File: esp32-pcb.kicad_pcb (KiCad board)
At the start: 2 copper layers, 25.2 x 59.4 mm, 47 parts, among them J1 Conn_01x15_Male, J2 Conn_01x15_Male, Q1 TSM2323CX, Q2 BSS138Q-7-F, Q3 MMBT3904, Q4 MMBT3904, SW1 RESET, SW2 USER, SW3 SW_DIP_x04, U1 TLV75533, U2 ESP32-WROOM-32, U3 CP2102N-A01-GQFN24

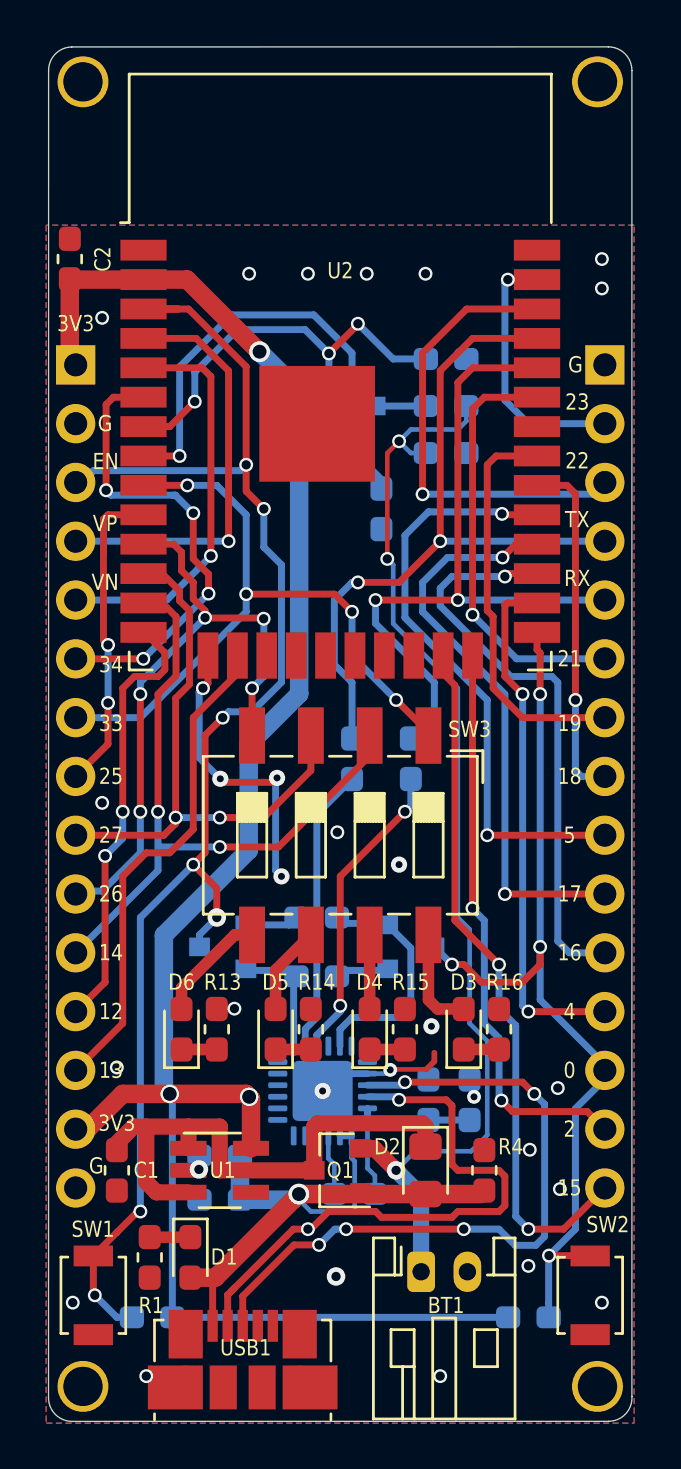
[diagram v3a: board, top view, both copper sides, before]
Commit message: Added TVS protection
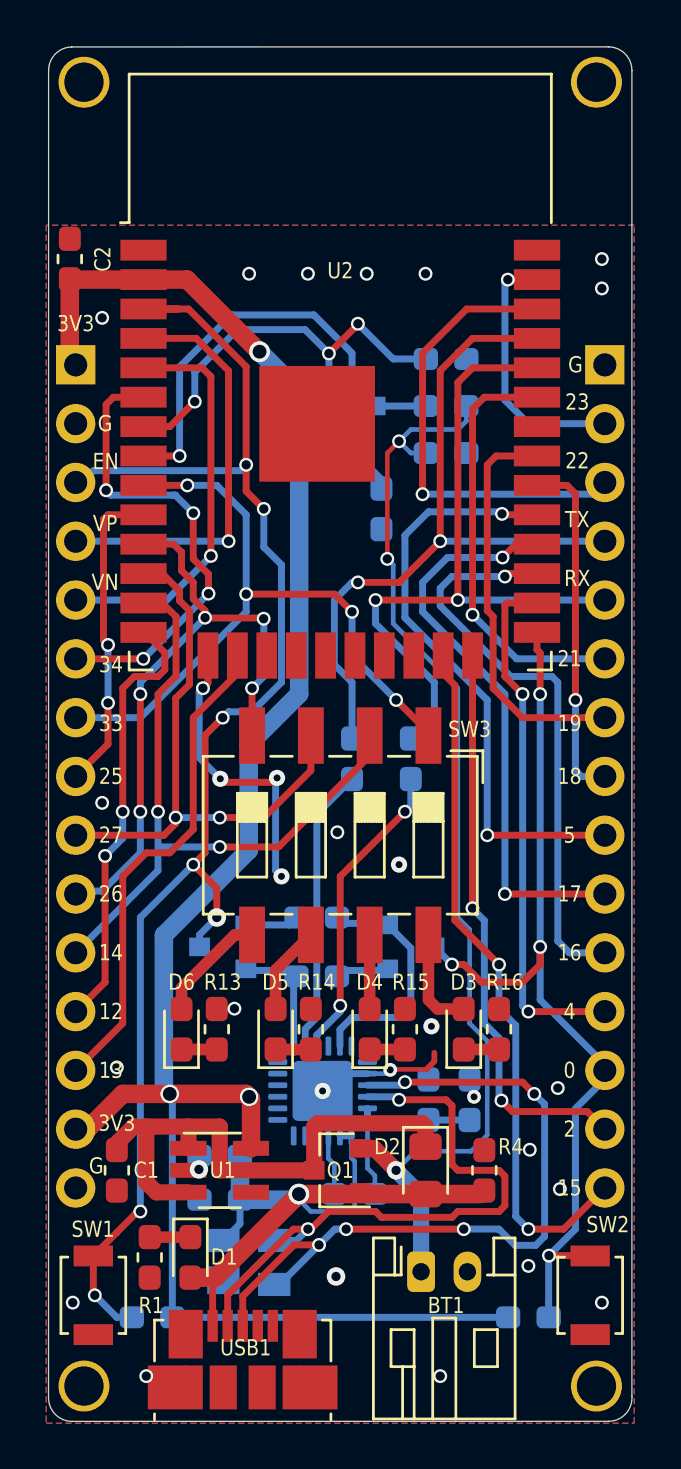
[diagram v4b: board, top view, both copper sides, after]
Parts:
- removed the REF** at (130.6, 126.2)
- removed the REF** at (152.8, 69.8)
- removed the REF** at (152.8, 126.2)
- removed the REF** at (130.6, 69.8)
- added D7: SP0503BAHT, Package_TO_SOT_SMD:SOT-143, B.Cu at (137.8, 120.8)
- added REF**: MountingHole_M1.7, esp32-pcb:MountingHole_M1.7, F.Cu at (152.8, 126.2)
- added REF**: MountingHole_M1.7, esp32-pcb:MountingHole_M1.7, F.Cu at (130.7, 126.2)
- added REF**: MountingHole_M1.7, esp32-pcb:MountingHole_M1.7, F.Cu at (130.7, 69.8)
- added REF**: MountingHole_M1.7, esp32-pcb:MountingHole_M1.7, F.Cu at (152.8, 69.8)
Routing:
- net USB_D+: track 29.9 -> 33.2 mm
- net 5V_USB: track 28.4 -> 30.4 mm
- net USB_D-: track 25.8 -> 27.5 mm
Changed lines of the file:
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@@
     (thickness 1.6)
     (drawings 3056)
-    (tracks 600)
+    (tracks 607)
     (zones 0)
-    (modules 47)
+    (modules 48)
     (nets 74)
   )
@@
   )
   (setup
-    (last_trace_width 0.25)
+    (last_trace_width 0.3)
     (user_trace_width 0.2)
     (user_trace_width 0.25)
@@
     (add_net V_BAT_MEASURE)
   )
-  (module esp32-pcb:MountingHole_M1.7 (layer F.Cu)
-    (at 130.6165 126.1745)
-    (fp_text reference REF** (at 0 -2.54) (layer F.SilkS) hide
+  (module esp32-pcb:MountingHole_M1.7 locked (layer F.Cu)
+    (at 152.8 126.16)
+    (fp_text reference REF** (at 0 -2.54) (layer Dwgs.User) hide
       (effects (font (size 1 1) (thickness 0.15)))
     )
@@
     (pad "" np_thru_hole circle (at 0 0) (size 2.2 2.2) (drill 1.7) (layers *.Cu *.Mask))
   )
-  (module esp32-pcb:MountingHole_M1.7 (layer F.Cu)
-    (at 152.8445 69.8145)
-    (fp_text reference REF** (at 0 -2.54) (layer F.SilkS) hide
+  (module esp32-pcb:MountingHole_M1.7 locked (layer F.Cu)
+    (at 130.66 126.16)
+    (fp_text reference REF** (at 0 -2.54) (layer Dwgs.User) hide
       (effects (font (size 1 1) (thickness 0.15)))
     )
@@
     (pad "" np_thru_hole circle (at 0 0) (size 2.2 2.2) (drill 1.7) (layers *.Cu *.Mask))
   )
-  (module esp32-pcb:MountingHole_M1.7 (layer F.Cu)
-    (at 152.8445 126.1745)
-    (fp_text reference REF** (at 0 -2.54) (layer F.SilkS) hide
+  (module esp32-pcb:MountingHole_M1.7 locked (layer F.Cu)
+    (at 130.66 69.83)
+    (fp_text reference REF** (at 0 -2.54) (layer Dwgs.User) hide
       (effects (font (size 1 1) (thickness 0.15)))
     )
@@
     (pad "" np_thru_hole circle (at 0 0) (size 2.2 2.2) (drill 1.7) (layers *.Cu *.Mask))
   )
-  (module esp32-pcb:MountingHole_M1.7 (layer F.Cu)
-    (at 130.6165 69.8145)
-    (fp_text reference REF** (at 0 -2.54) (layer F.SilkS) hide
+  (module esp32-pcb:MountingHole_M1.7 locked (layer F.Cu)
+    (at 152.8 69.83)
+    (fp_text reference REF** (at 0 -2.54) (layer Dwgs.User) hide
       (effects (font (size 1 1) (thickness 0.15)))
     )
@@
     (pad "" np_thru_hole circle (at 0 0) (size 2.2 2.2) (drill 1.7) (layers *.Cu *.Mask))
   )
+  (module Package_TO_SOT_SMD:SOT-143 (layer B.Cu)
+    (at 137.78 120.82)
+    (descr SOT-143)
+    (tags SOT-143)
+    (attr smd)
+    (fp_text reference D7 (at -0.084 2.1615) (layer B.SilkS)
+      (effects (font (size 0.7 0.6) (thickness 0.15)) (justify mirror))
+    )
+    (fp_text value SP0503BAHT (at -0.28 -2.48) (layer B.Fab)
+      (effects (font (size 1 1) (thickness 0.15)) (justify mirror))
+    )
+    (fp_line (start -2.05 -1.75) (end -2.05 1.75) (layer B.CrtYd) (width 0.05))
+    (fp_line (start -2.05 -1.75) (end 2.05 -1.75) (layer B.CrtYd) (width 0.05))
+    (fp_line (start 2.05 1.75) (end -2.05 1.75) (layer B.CrtYd) (width 0.05))
+    (fp_line (start 2.05 1.75) (end 2.05 -1.75) (layer B.CrtYd) (width 0.05))
+    (fp_line (start 1.2 1.5) (end 1.2 -1.5) (layer B.Fab) (width 0.1))
+    (fp_line (start 1.2 -1.5) (end -1.2 -1.5) (layer B.Fab) (width 0.1))
+    (fp_line (start -1.2 -1.5) (end -1.2 1) (layer B.Fab) (width 0.1))
+    (fp_line (start -0.7 1.5) (end 1.2 1.5) (layer B.Fab) (width 0.1))
+    (fp_line (start -1.2 1) (end -0.7 1.5) (layer B.Fab) (width 0.1))
+    (fp_line (start 1.2 1.55) (end -1.75 1.55) (layer B.SilkS) (width 0.12))
+    (fp_line (start -1.2 -1.55) (end 1.2 -1.55) (layer B.SilkS) (width 0.12))
+    (fp_text user %R (at 0 0 -90) (layer B.Fab)
+      (effects (font (size 0.5 0.5) (thickness 0.075)) (justify mirror))
+    )
+    (pad 4 smd rect (at 1.1 0.95 90) (size 1 1.4) (layers B.Cu B.Paste B.Mask)
+      (net 70 USB_D+))
+    (pad 3 smd rect (at 1.1 -0.95 90) (size 1 1.4) (layers B.Cu B.Paste B.Mask)
+      (net 69 USB_D-))
+    (pad 2 smd rect (at -1.1 -0.95 90) (size 1 1.4) (layers B.Cu B.Paste B.Mask)
+      (net 5 5V_USB))
+    (pad 1 smd rect (at -1.1 0.77 90) (size 1.2 1.4) (layers B.Cu B.Paste B.Mask)
+      (net 1 GND))
+    (model ${KISYS3DMOD}/Package_TO_SOT_SMD.3dshapes/SOT-143.wrl
+      (at (xyz 0 0 0))
+      (scale (xyz 1 1 1))
+      (rotate (xyz 0 0 0))
+    )
+  )
   (module Package_TO_SOT_SMD:SOT-23-5_HandSoldering (layer F.Cu)
     (at 136.525 116.84)
@@
   (segment (start 136.335 121.475) (end 135.255 121.475) (width 0.8) (layer F.Cu) (net 5))
   (segment (start 139.945 117.865) (end 136.335 121.475) (width 0.8) (layer F.Cu) (net 5))
+  (segment (start 137.4 119.15) (end 136.68 119.87) (width 0.3) (layer B.Cu) (net 5))
+  (segment (start 137.4 118.11) (end 137.4 119.15) (width 0.3) (layer B.Cu) (net 5))
   (segment (start 133.5 119.725) (end 135.255 119.725) (width 0.5) (layer F.Cu) (net 6) (status 30))
   (segment (start 147.066 109.869) (end 145.937 109.869) (width 0.5) (layer F.Cu) (net 7) (status 10))
@@
   (segment (start 137.026041 122.062) (end 137.16402 121.92402) (width 0.3) (layer F.Cu) (net 69))
   (segment (start 137.16402 121.92402) (end 139.708041 119.38) (width 0.3) (layer F.Cu) (net 69))
+  (segment (start 139.845 119.87) (end 140.335 119.38) (width 0.3) (layer B.Cu) (net 69))
+  (segment (start 138.88 119.87) (end 139.845 119.87) (width 0.3) (layer B.Cu) (net 69))
   (via (at 140.814952 120.062931) (size 0.6) (drill 0.4) (layers F.Cu B.Cu) (net 70))
   (segment (start 140.922069 120.062931) (end 140.814952 120.062931) (width 0.3) (layer B.Cu) (net 70))
@@
   (segment (start 150.114 113.538) (end 150.5585 113.9825) (width 0.3) (layer B.Cu) (net 70))
   (segment (start 150.5585 113.9825) (end 150.5585 119.6975) (width 0.3) (layer B.Cu) (net 70))
+  (segment (start 138.344 121.8515) (end 139.026383 121.8515) (width 0.3) (layer B.Cu) (net 70))
+  (segment (start 139.107883 121.77) (end 140.814952 120.062931) (width 0.3) (layer B.Cu) (net 70))
+  (segment (start 138.88 121.77) (end 139.107883 121.77) (width 0.3) (layer B.Cu) (net 70))
   (segment (start 145.288 114.808) (end 140.748 114.808) (width 0.7) (layer F.Cu) (net 73))
   (segment (start 132.08 115.965) (end 132.08 115.67) (width 0.5) (layer F.Cu) (net 73) (status 30))
